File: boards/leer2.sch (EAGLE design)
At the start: 64 parts, among them IC2 7805DT, Q1 BC846BSMD, Q2 BC846BSMD, Q3 BC846BSMD, Q4 BC846BSMD, Q5 BC846BSMD, Q6 BC846BSMD, Q7 BC846BSMD, Q8 BC846BSMD

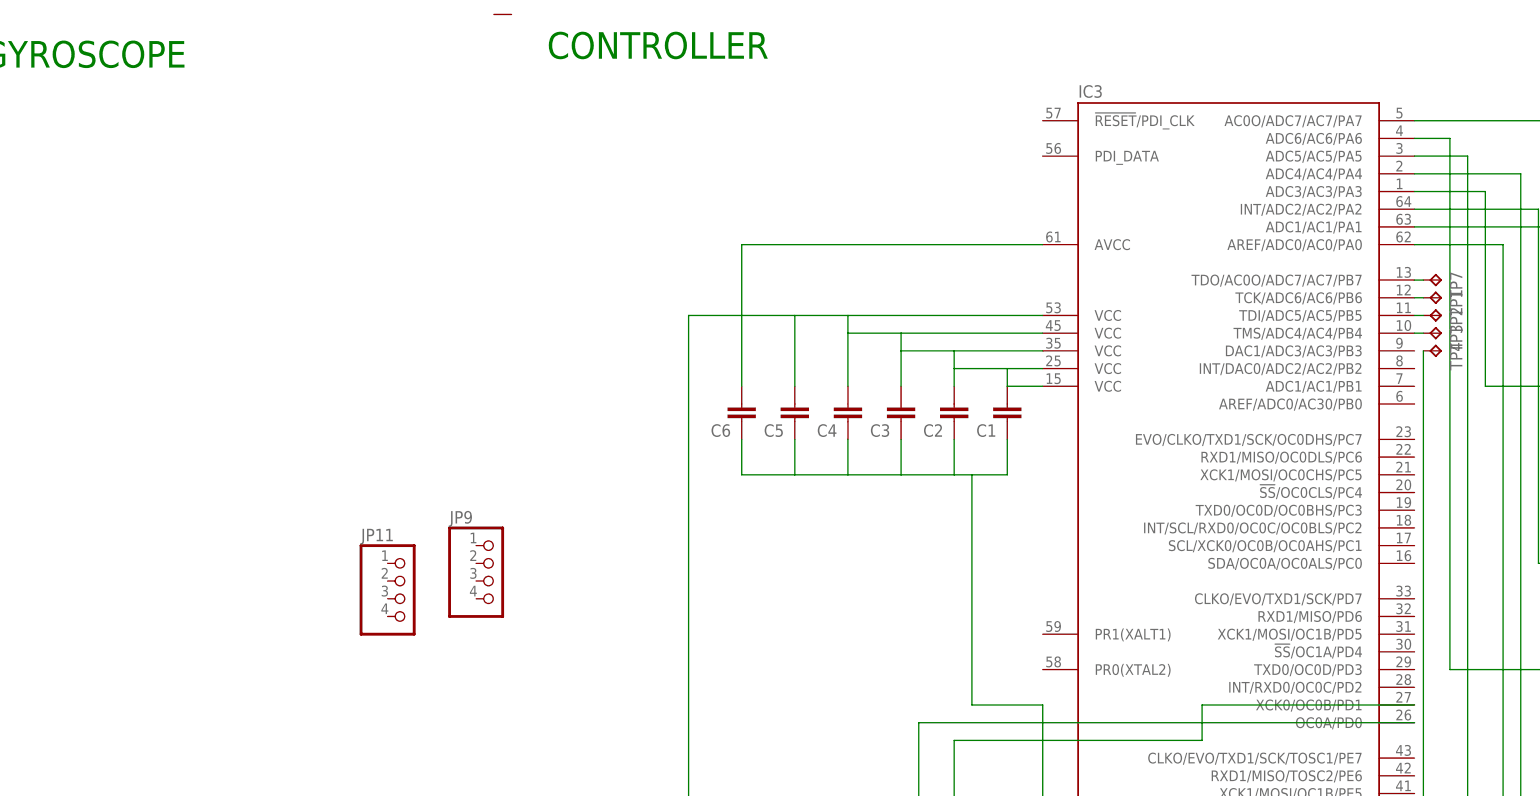
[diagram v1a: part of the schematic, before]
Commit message: Updated Board with Voltage-Sensing Circuit
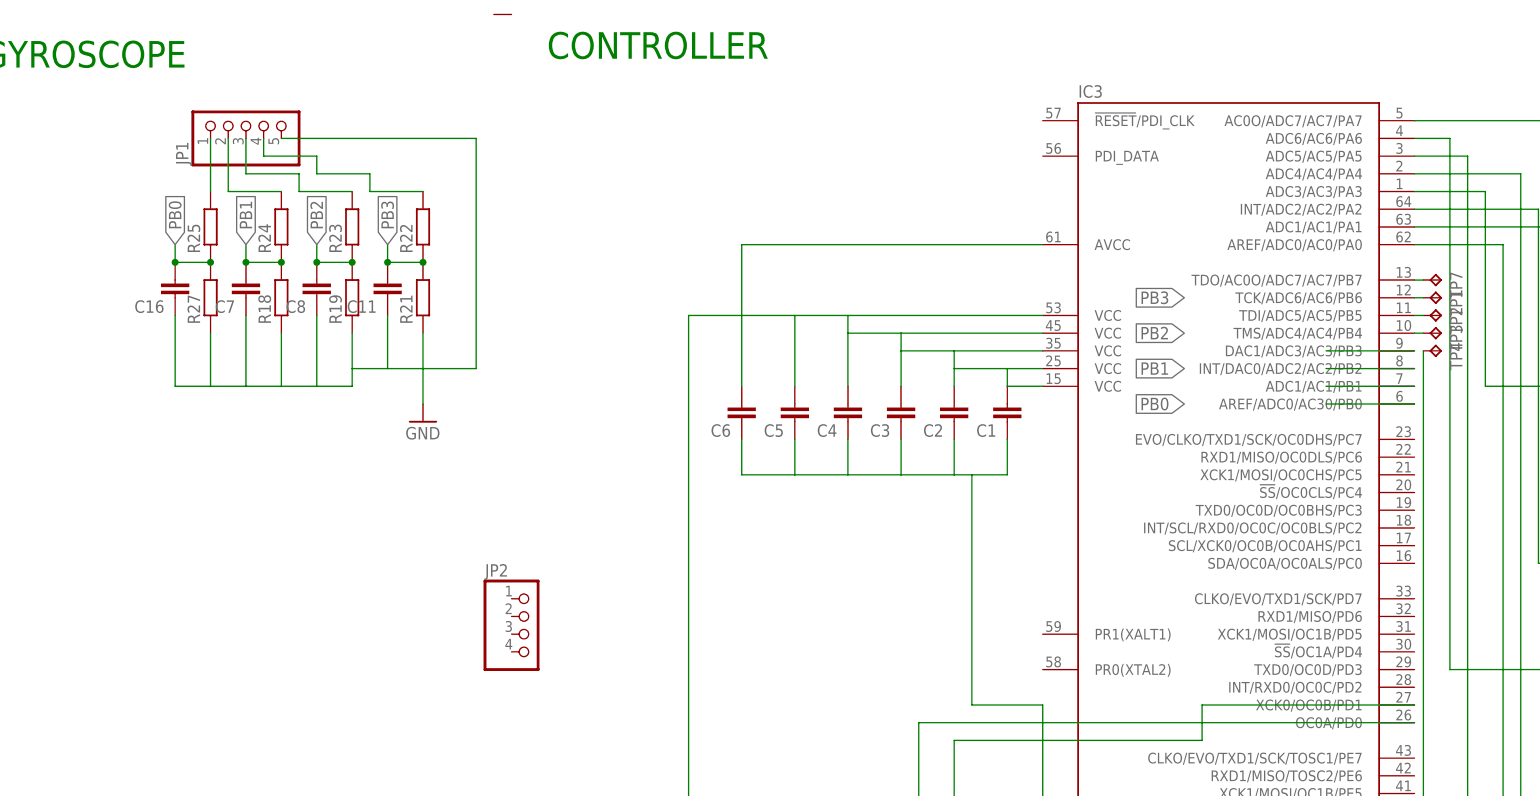
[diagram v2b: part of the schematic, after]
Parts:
- removed JP11, JP9: (no value), pinhead:PINHD-1X4
- added C11, C16, C7, C8: (no value), eagle-ltspice:CC0603
- added JP1: (no value), pinhead:PINHD-1X5/90
- added JP2: (no value), pinhead:PINHD-1X4/90
- added R18, R19, R21, R22, R23, R24, R25, R27: (no value), eagle-ltspice:RR0603
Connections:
- new net N$42: JP1.2, R24.2
- new net N$43: JP1.3, R23.2
- new net N$44: JP1.4, R22.2
- new net N$50: JP1.1, R25.2
- new net PB0: C16.2, IC3.AREF/ADC0/AC30/PB0, R25.1, R27.2
- new net PB1: C7.2, IC3.ADC1/AC1/PB1, R18.2, R24.1
- new net PB2: C8.2, IC3.INT/DAC0/ADC2/AC2/PB2, R19.2, R23.1
- new net PB3: C11.2, IC3.DAC1/ADC3/AC3/PB3, R21.2, R22.1
- net GND: now also C11.1, C16.1, C7.1, C8.1, JP1.5, R18.1, R19.1, R21.1, R27.1
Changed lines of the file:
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@@
 <part name="IC2" library="linear" deviceset="78*" device="DT" technology="05"/>
 <part name="FRAME1" library="frames" deviceset="A3L-LOC" device=""/>
-<part name="JP11" library="pinhead" deviceset="PINHD-1X4" device=""/>
-<part name="JP9" library="pinhead" deviceset="PINHD-1X4" device=""/>
 <part name="Q4" library="transistor-npn" deviceset="BC846*" device="SMD" technology="B"/>
 <part name="BEC04" library="pinhead" deviceset="PINHD-1X3" device="" value="PCM"/>
@@
 <part name="TP3" library="testpad" deviceset="TP" device="TP08R"/>
 <part name="TP4" library="testpad" deviceset="TP" device="TP08R"/>
+<part name="JP1" library="pinhead" deviceset="PINHD-1X5" device="/90"/>
+<part name="JP2" library="pinhead" deviceset="PINHD-1X4" device="/90"/>
+<part name="GND6" library="supply1" deviceset="GND" device=""/>
+<part name="R27" library="eagle-ltspice" deviceset="R" device="R0603"/>
+<part name="R18" library="eagle-ltspice" deviceset="R" device="R0603"/>
+<part name="R19" library="eagle-ltspice" deviceset="R" device="R0603"/>
+<part name="R21" library="eagle-ltspice" deviceset="R" device="R0603"/>
+<part name="R22" library="eagle-ltspice" deviceset="R" device="R0603"/>
+<part name="R23" library="eagle-ltspice" deviceset="R" device="R0603"/>
+<part name="R24" library="eagle-ltspice" deviceset="R" device="R0603"/>
+<part name="R25" library="eagle-ltspice" deviceset="R" device="R0603"/>
+<part name="C16" library="eagle-ltspice" deviceset="C" device="C0603"/>
+<part name="C7" library="eagle-ltspice" deviceset="C" device="C0603"/>
+<part name="C8" library="eagle-ltspice" deviceset="C" device="C0603"/>
+<part name="C11" library="eagle-ltspice" deviceset="C" device="C0603"/>
 </parts>
 <sheets>
@@
 <instance part="IC2" gate="A1" x="342.9" y="68.58"/>
 <instance part="FRAME1" gate="G$1" x="0" y="0"/>
-<instance part="JP11" gate="A" x="116.84" y="172.72"/>
-<instance part="JP9" gate="A" x="129.54" y="175.26"/>
 <instance part="Q4" gate="G$1" x="297.18" y="218.44"/>
 <instance part="BEC04" gate="A" x="325.12" y="226.06"/>
@@
 <instance part="TP3" gate="G$1" x="265.43" y="210.82" rot="R270"/>
 <instance part="TP4" gate="G$1" x="265.43" y="208.28" rot="R270"/>
+<instance part="JP1" gate="A" x="93.98" y="241.3" rot="R90"/>
+<instance part="JP2" gate="A" x="134.62" y="167.64"/>
+<instance part="GND6" gate="1" x="119.38" y="198.12"/>
+<instance part="R27" gate="G$1" x="88.9" y="215.9" rot="R90"/>
+<instance part="R18" gate="G$1" x="99.06" y="215.9" rot="R90"/>
+<instance part="R19" gate="G$1" x="109.22" y="215.9" rot="R90"/>
+<instance part="R21" gate="G$1" x="119.38" y="215.9" rot="R90"/>
+<instance part="R22" gate="G$1" x="119.38" y="226.06" rot="R90"/>
+<instance part="R23" gate="G$1" x="109.22" y="226.06" rot="R90"/>
+<instance part="R24" gate="G$1" x="99.06" y="226.06" rot="R90"/>
+<instance part="R25" gate="G$1" x="88.9" y="226.06" rot="R90"/>
+<instance part="C16" gate="G$1" x="83.82" y="215.9" rot="R180"/>
+<instance part="C7" gate="G$1" x="93.98" y="215.9" rot="R180"/>
+<instance part="C8" gate="G$1" x="104.14" y="215.9" rot="R180"/>
+<instance part="C11" gate="G$1" x="114.3" y="215.9" rot="R180"/>
 </instances>
 <busses>
@@
 <pinref part="GND15" gate="1" pin="GND"/>
 </segment>
+<segment>
+<wire x1="93.98" y1="213.36" x2="93.98" y2="203.2" width="0.1524" layer="91"/>
+<wire x1="83.82" y1="213.36" x2="83.82" y2="203.2" width="0.1524" layer="91"/>
+<wire x1="88.9" y1="210.82" x2="88.9" y2="203.2" width="0.1524" layer="91"/>
+<wire x1="83.82" y1="203.2" x2="88.9" y2="203.2" width="0.1524" layer="91"/>
+<wire x1="93.98" y1="203.2" x2="88.9" y2="203.2" width="0.1524" layer="91"/>
+<wire x1="99.06" y1="210.82" x2="99.06" y2="203.2" width="0.1524" layer="91"/>
+<wire x1="93.98" y1="203.2" x2="99.06" y2="203.2" width="0.1524" layer="91"/>
+<wire x1="104.14" y1="213.36" x2="104.14" y2="203.2" width="0.1524" layer="91"/>
+<wire x1="99.06" y1="203.2" x2="104.14" y2="203.2" width="0.1524" layer="91"/>
+<wire x1="109.22" y1="210.82" x2="109.22" y2="205.74" width="0.1524" layer="91"/>
+<wire x1="104.14" y1="203.2" x2="109.22" y2="203.2" width="0.1524" layer="91"/>
+<wire x1="109.22" y1="203.2" x2="109.22" y2="205.74" width="0.1524" layer="91"/>
+<wire x1="114.3" y1="213.36" x2="114.3" y2="205.74" width="0.1524" layer="91"/>
+<wire x1="109.22" y1="205.74" x2="114.3" y2="205.74" width="0.1524" layer="91"/>
+<pinref part="GND6" gate="1" pin="GND"/>
+<wire x1="119.38" y1="210.82" x2="119.38" y2="205.74" width="0.1524" layer="91"/>
+<wire x1="119.38" y1="205.74" x2="119.38" y2="200.66" width="0.1524" layer="91"/>
+<wire x1="114.3" y1="205.74" x2="119.38" y2="205.74" width="0.1524" layer="91"/>
+<wire x1="119.38" y1="205.74" x2="127" y2="205.74" width="0.1524" layer="91"/>
+<wire x1="127" y1="205.74" x2="127" y2="238.76" width="0.1524" layer="91"/>
+<pinref part="JP1" gate="A" pin="5"/>
+<wire x1="127" y1="238.76" x2="99.06" y2="238.76" width="0.1524" layer="91"/>
+<pinref part="R27" gate="G$1" pin="1"/>
+<pinref part="R18" gate="G$1" pin="1"/>
+<pinref part="R19" gate="G$1" pin="1"/>
+<pinref part="R21" gate="G$1" pin="1"/>
+<pinref part="C16" gate="G$1" pin="1"/>
+<pinref part="C7" gate="G$1" pin="1"/>
+<pinref part="C8" gate="G$1" pin="1"/>
+<pinref part="C11" gate="G$1" pin="1"/>
+</segment>
 </net>
 <net name="N$37" class="0">
@@
 </segment>
 </net>
+<net name="N$50" class="0">
+<segment>
+<wire x1="88.9" y1="238.76" x2="88.9" y2="231.14" width="0.1524" layer="91"/>
+<pinref part="JP1" gate="A" pin="1"/>
+<pinref part="R25" gate="G$1" pin="2"/>
+</segment>
+</net>
+<net name="PB1" class="0">
+<segment>
+<pinref part="IC3" gate="G$1" pin="ADC1/AC1/PB1"/>
+<wire x1="261.62" y1="203.2" x2="248.92" y2="203.2" width="0.1524" layer="91"/>
+<label x="228.6" y="205.74" size="1.778" layer="95" rot="R180" xref="yes"/>
+</segment>
+<segment>
+<wire x1="99.06" y1="220.98" x2="93.98" y2="220.98" width="0.1524" layer="91"/>
+<wire x1="93.98" y1="220.98" x2="93.98" y2="223.52" width="0.1524" layer="91"/>
+<label x="93.98" y="223.52" size="1.778" layer="95" rot="R90" xref="yes"/>
+<pinref part="R18" gate="G$1" pin="2"/>
+<pinref part="R24" gate="G$1" pin="1"/>
+<junction x="99.06" y="220.98"/>
+<pinref part="C7" gate="G$1" pin="2"/>
+<junction x="93.98" y="220.98"/>
+</segment>
+</net>
+<net name="PB2" class="0">
+<segment>
+<pinref part="IC3" gate="G$1" pin="INT/DAC0/ADC2/AC2/PB2"/>
+<wire x1="261.62" y1="205.74" x2="248.92" y2="205.74" width="0.1524" layer="91"/>
+<label x="228.6" y="210.82" size="1.778" layer="95" rot="R180" xref="yes"/>
+</segment>
+<segment>
+<wire x1="109.22" y1="220.98" x2="104.14" y2="220.98" width="0.1524" layer="91"/>
+<wire x1="104.14" y1="220.98" x2="104.14" y2="223.52" width="0.1524" layer="91"/>
+<label x="104.14" y="223.52" size="1.778" layer="95" rot="R90" xref="yes"/>
+<pinref part="R19" gate="G$1" pin="2"/>
+<pinref part="R23" gate="G$1" pin="1"/>
+<junction x="109.22" y="220.98"/>
+<pinref part="C8" gate="G$1" pin="2"/>
+<junction x="104.14" y="220.98"/>
+</segment>
+</net>
+<net name="PB3" class="0">
+<segment>
+<pinref part="IC3" gate="G$1" pin="DAC1/ADC3/AC3/PB3"/>
+<wire x1="261.62" y1="208.28" x2="248.92" y2="208.28" width="0.1524" layer="91"/>
+<label x="228.6" y="215.9" size="1.778" layer="95" rot="R180" xref="yes"/>
+</segment>
+<segment>
+<wire x1="119.38" y1="220.98" x2="114.3" y2="220.98" width="0.1524" layer="91"/>
+<wire x1="114.3" y1="220.98" x2="114.3" y2="223.52" width="0.1524" layer="91"/>
+<label x="114.3" y="223.52" size="1.778" layer="95" rot="R90" xref="yes"/>
+<pinref part="R21" gate="G$1" pin="2"/>
+<pinref part="R22" gate="G$1" pin="1"/>
+<junction x="119.38" y="220.98"/>
+<pinref part="C11" gate="G$1" pin="2"/>
+<junction x="114.3" y="220.98"/>
+</segment>
+</net>
+<net name="N$42" class="0">
+<segment>
+<pinref part="JP1" gate="A" pin="2"/>
+<wire x1="99.06" y1="231.14" x2="91.44" y2="231.14" width="0.1524" layer="91"/>
+<wire x1="91.44" y1="231.14" x2="91.44" y2="238.76" width="0.1524" layer="91"/>
+<pinref part="R24" gate="G$1" pin="2"/>
+</segment>
+</net>
+<net name="N$43" class="0">
+<segment>
+<wire x1="109.22" y1="231.14" x2="101.6" y2="231.14" width="0.1524" layer="91"/>
+<wire x1="101.6" y1="231.14" x2="101.6" y2="233.68" width="0.1524" layer="91"/>
+<pinref part="JP1" gate="A" pin="3"/>
+<wire x1="101.6" y1="233.68" x2="93.98" y2="233.68" width="0.1524" layer="91"/>
+<wire x1="93.98" y1="233.68" x2="93.98" y2="238.76" width="0.1524" layer="91"/>
+<pinref part="R23" gate="G$1" pin="2"/>
+</segment>
+</net>
+<net name="N$44" class="0">
+<segment>
+<wire x1="119.38" y1="231.14" x2="111.76" y2="231.14" width="0.1524" layer="91"/>
+<wire x1="111.76" y1="231.14" x2="111.76" y2="233.68" width="0.1524" layer="91"/>
+<wire x1="111.76" y1="233.68" x2="104.14" y2="233.68" width="0.1524" layer="91"/>
+<wire x1="104.14" y1="233.68" x2="104.14" y2="236.22" width="0.1524" layer="91"/>
+<pinref part="JP1" gate="A" pin="4"/>
+<wire x1="104.14" y1="236.22" x2="96.52" y2="236.22" width="0.1524" layer="91"/>
+<wire x1="96.52" y1="236.22" x2="96.52" y2="238.76" width="0.1524" layer="91"/>
+<pinref part="R22" gate="G$1" pin="2"/>
+</segment>
+</net>
+<net name="PB0" class="0">
+<segment>
+<pinref part="IC3" gate="G$1" pin="AREF/ADC0/AC30/PB0"/>
+<wire x1="261.62" y1="200.66" x2="248.92" y2="200.66" width="0.1524" layer="91"/>
+<label x="228.6" y="200.66" size="1.778" layer="95" rot="R180" xref="yes"/>
+</segment>
+<segment>
+<wire x1="88.9" y1="220.98" x2="83.82" y2="220.98" width="0.1524" layer="91"/>
+<wire x1="83.82" y1="220.98" x2="83.82" y2="223.52" width="0.1524" layer="91"/>
+<label x="83.82" y="223.52" size="1.778" layer="95" rot="R90" xref="yes"/>
+<pinref part="R27" gate="G$1" pin="2"/>
+<pinref part="R25" gate="G$1" pin="1"/>
+<junction x="88.9" y="220.98"/>
+<pinref part="C16" gate="G$1" pin="2"/>
+<junction x="83.82" y="220.98"/>
+</segment>
+</net>
